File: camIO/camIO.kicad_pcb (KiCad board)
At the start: 4 copper layers, 30 x 30 mm, 37 parts, among them IC3 TLV61225DC, J6 MISC, J8 CSI/DSI, Q1 BSS138, U1 PCA9306

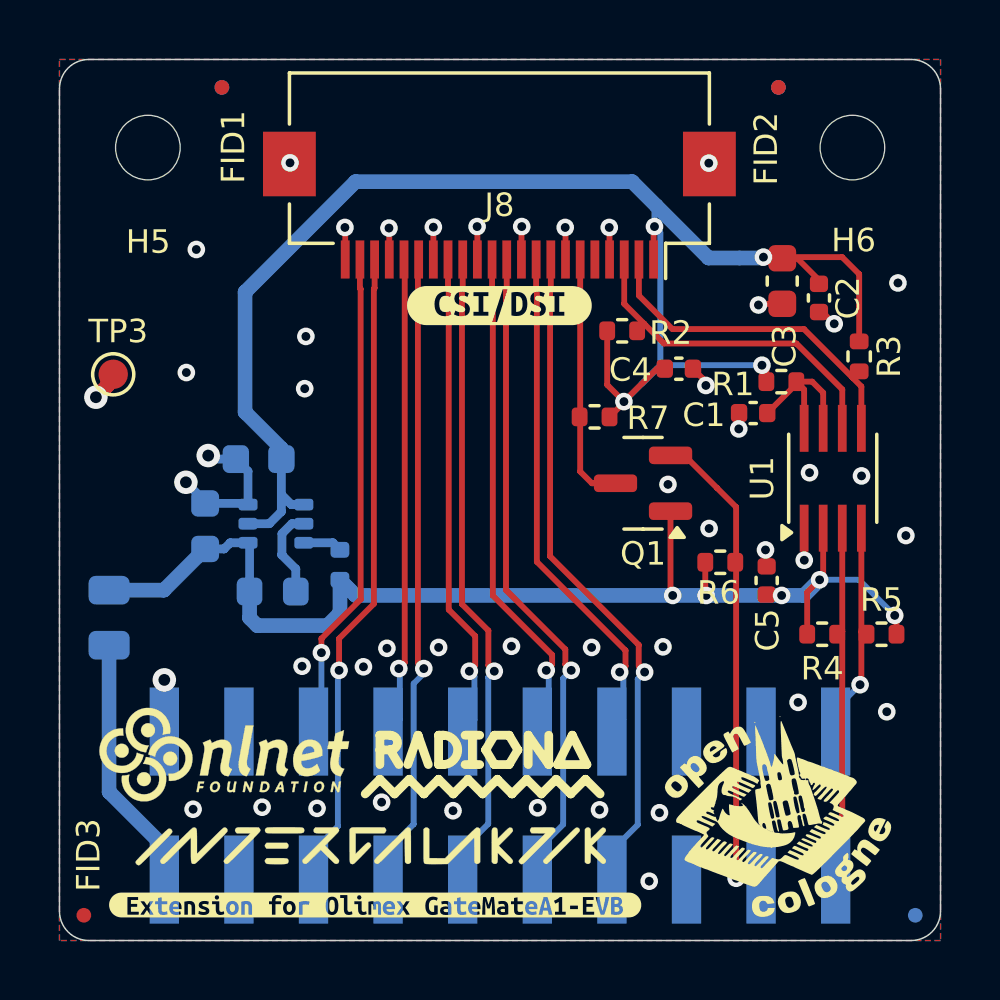
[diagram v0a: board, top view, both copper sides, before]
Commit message: Removing U1 as it is not needed - #4
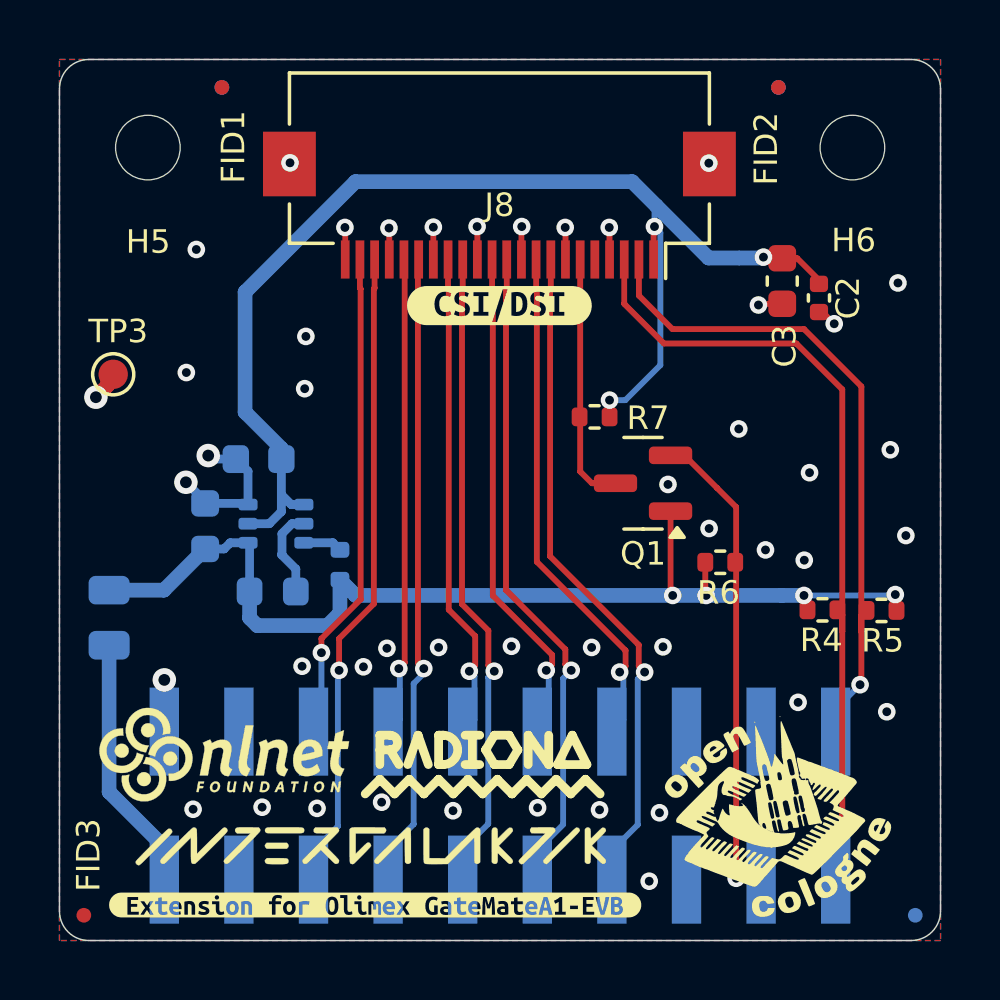
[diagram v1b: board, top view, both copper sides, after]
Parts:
- removed C1: 470p, Capacitor_SMD:C_0402_1005Metric
- removed C4, C5: 100n, Capacitor_SMD:C_0402_1005Metric
- removed R1: 100K, Resistor_SMD:R_0402_1005Metric
- removed R2, R3: 4k7, Resistor_SMD:R_0402_1005Metric
- removed U1: PCA9306, Package_SO:SSOP-8_2.95x2.8mm_P0.65mm
- moved R4 0.83 mm to (111.2, 70.6)
- moved R5 0.81 mm to (113.2, 70.6)
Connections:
- J8 pad 2: /Main Sheet/SDA0 -> /Main Sheet/NB_B8_8N
- J8 pad 3: /Main Sheet/SCL0 -> /Main Sheet/NB_A8_8P
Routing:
- net +VCC_HIGH: track 57.9 -> 42.3 mm, vias 4 -> 3
- net /Main Sheet/NB_B8_8N: track 7.50 -> 23.0 mm
- net /Main Sheet/NB_A8_8P: track 12.5 -> 28.0 mm
- net /Main Sheet/SDA0: track 11.8 -> 0.00 mm
- net /Main Sheet/SCL0: track 11.8 -> 0.00 mm
- net /Main Sheet/VREF2: track 5.47 -> 0.00 mm
- net +VCC_LOW: track 41.4 -> 36.8 mm, vias 5 -> 4
- net GND: track 20.1 -> 17.2 mm, vias 47 -> 46

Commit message: sch cleanup - reference cleanup
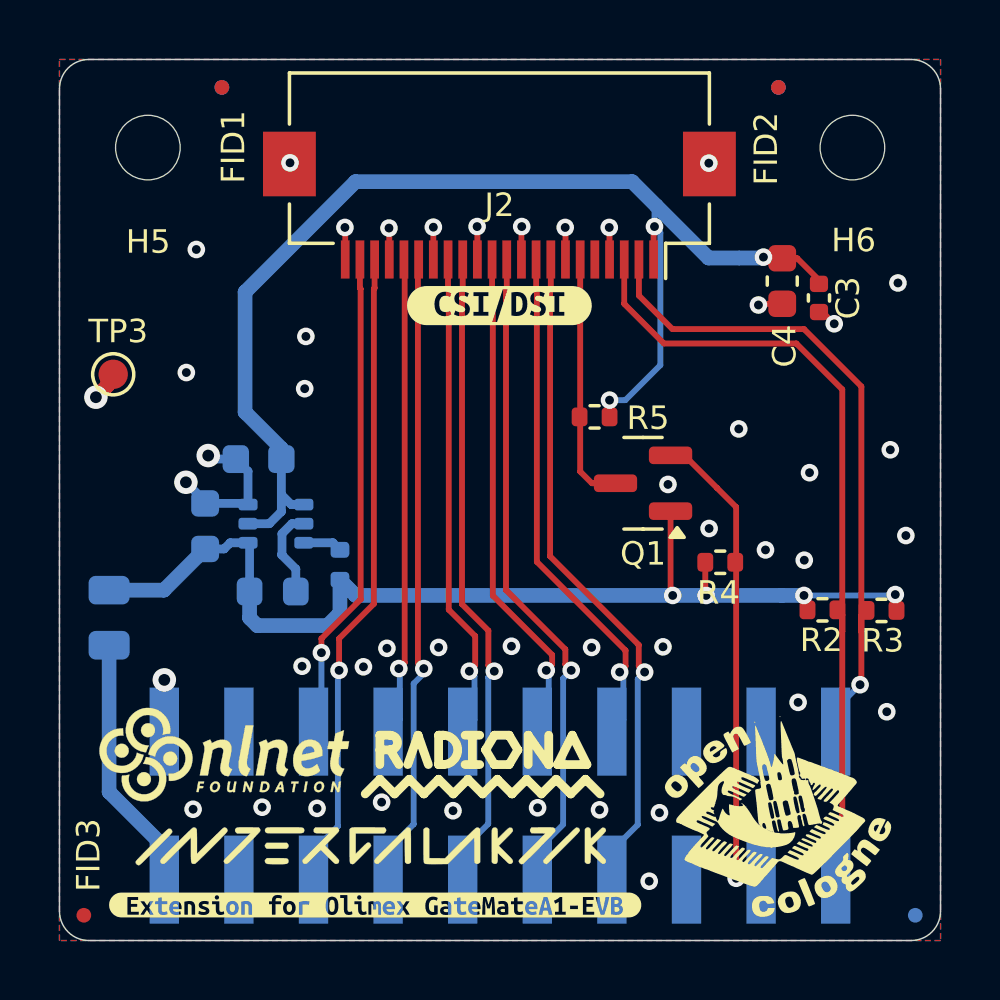
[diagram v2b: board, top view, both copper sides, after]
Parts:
- renumbered C13 to C1, C14 to C2, C2 to C3, C3 to C4, IC3 to IC1, J6 to J1, J8 to J2, R15 to R1, R4 to R2, R5 to R3, R6 to R4, R7 to R5
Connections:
- net /Main Sheet/CAM_C_N renamed /Main Sheet/NB_B3_3N
- net /Main Sheet/CAM_C_P renamed /Main Sheet/NB_A3_3P
- net /Main Sheet/CAM_D0_N renamed /Main Sheet/NB_B1_1N
- net /Main Sheet/CAM_D0_P renamed /Main Sheet/NB_A1_1P
- net /Main Sheet/CAM_D1_N renamed /Main Sheet/NB_B2_2N
- net /Main Sheet/CAM_D1_P renamed /Main Sheet/NB_A2_2P
- net /Main Sheet/CAM_D2_N renamed /Main Sheet/NB_B4_4N
- net /Main Sheet/CAM_D2_P renamed /Main Sheet/NB_A4_4P
- net /Main Sheet/CAM_D3_N renamed /Main Sheet/NB_B5_5N
- net /Main Sheet/CAM_D3_P renamed /Main Sheet/NB_A5_5P

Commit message: Adding LP pins on P side of diff pair #4
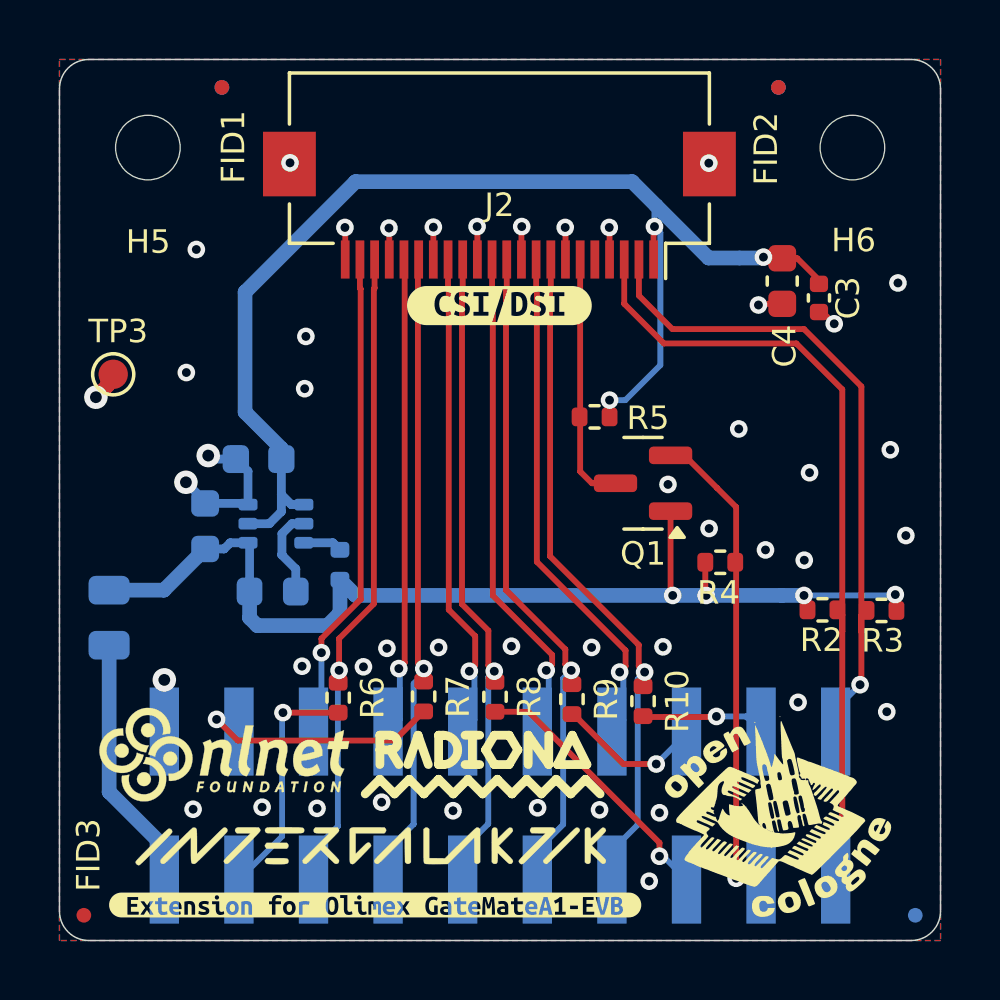
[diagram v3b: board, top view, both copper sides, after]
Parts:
- added R10: 3k3, Resistor_SMD:R_0402_1005Metric, F.Cu at (105.1, 73.7)
- added R6: 3k3, Resistor_SMD:R_0402_1005Metric, F.Cu at (94.7, 73.6)
- added R7: 3k3, Resistor_SMD:R_0402_1005Metric, F.Cu at (97.7, 73.5)
- added R8: 3k3, Resistor_SMD:R_0402_1005Metric, F.Cu at (100.1, 73.5)
- added R9: 3k3, Resistor_SMD:R_0402_1005Metric, F.Cu at (102.7, 73.6)
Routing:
- net /Main Sheet/NB_A6_6P: track 0.00 -> 9.16 mm, vias 0 -> 1
- net /Main Sheet/NB_B0_0N: track 0.00 -> 8.69 mm, vias 0 -> 1
- net /Main Sheet/NB_A0_0P: track 0.00 -> 8.19 mm, vias 0 -> 1
- net /Main Sheet/NB_B6_6N: track 0.00 -> 5.11 mm, vias 0 -> 1
- net /Main Sheet/NB_B7_7N: track 0.00 -> 4.25 mm, vias 0 -> 1

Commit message: Adding termination #4
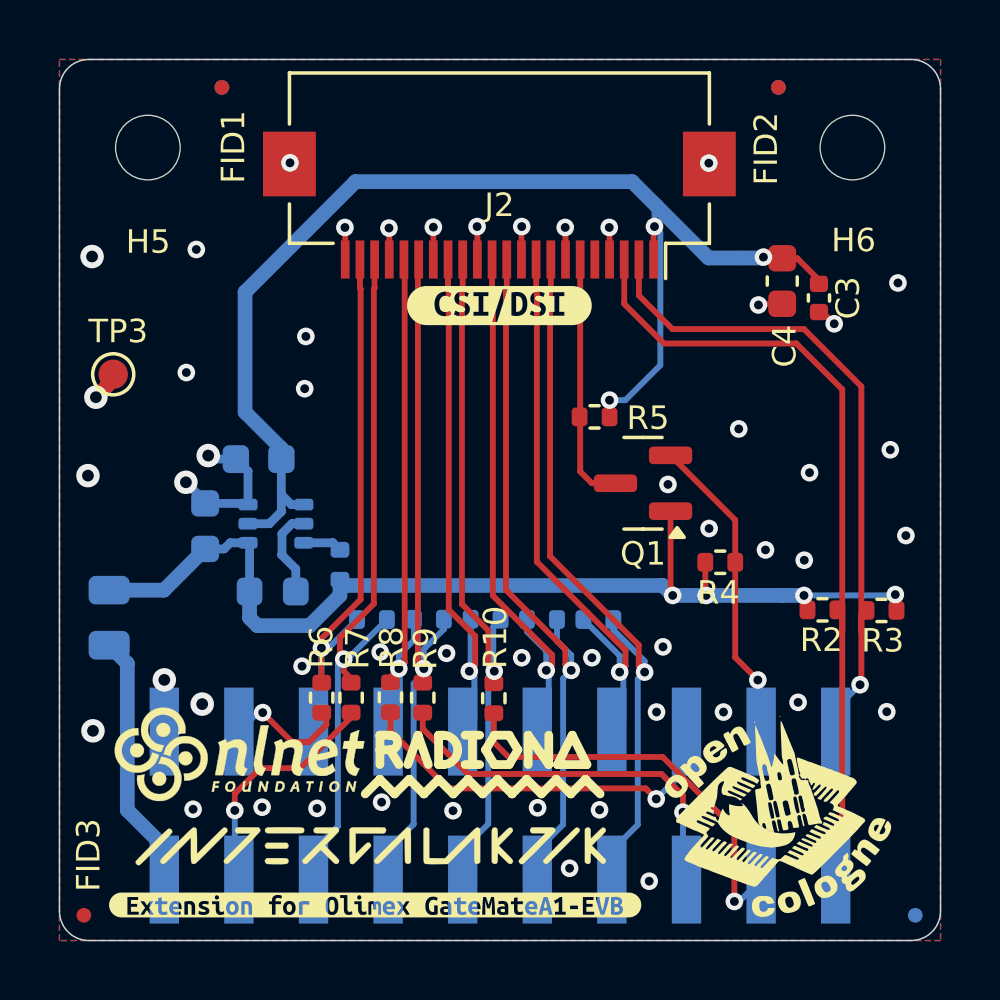
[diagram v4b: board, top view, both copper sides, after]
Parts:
- added R11: 100, Resistor_SMD:R_0402_1005Metric, B.Cu at (95.9, 70.9)
- added R12: 100, Resistor_SMD:R_0402_1005Metric, B.Cu at (97.8, 70.9)
- added R13: 100, Resistor_SMD:R_0402_1005Metric, B.Cu at (99.8, 70.9)
- added R14: 100, Resistor_SMD:R_0402_1005Metric, B.Cu at (101.7, 70.9)
- added R15: 100, Resistor_SMD:R_0402_1005Metric, B.Cu at (103.6, 70.9)
- R10, R6, R7, R8, R9: value 3k3 -> 100
- moved R10 5.08 mm to (100.0, 73.6)
- moved R9 5.08 mm to (97.6, 73.6)
- moved R8 3.56 mm to (96.5, 73.6)
- moved R7 2.47 mm to (95.2, 73.6)
- moved R6 0.56 mm to (94.2, 73.6)
- moved H2 0.52 mm to (91.4, 75.5)
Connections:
- Q1 pad 2: /Main Sheet/NB_A7_7P -> /Main Sheet/NB_B7_7N
- R10 pad 1: /Main Sheet/NB_A5_5P -> /Main Sheet/NB_A3_3P
- R10 pad 2: /Main Sheet/NB_B7_7N -> /Main Sheet/NB_A7_7P
- R4 pad 1: /Main Sheet/NB_A7_7P -> /Main Sheet/NB_B7_7N
- R6 pad 1: /Main Sheet/NB_A1_1P -> /Main Sheet/NB_B1_1N
- R6 pad 2: /Main Sheet/NB_A0_0P -> /Main Sheet/NB_B0_0N
- R7 pad 1: /Main Sheet/NB_A2_2P -> /Main Sheet/NB_A1_1P
- R7 pad 2: /Main Sheet/NB_B0_0N -> /Main Sheet/NB_A0_0P
- R8 pad 1: /Main Sheet/NB_A3_3P -> /Main Sheet/NB_B2_2N
- R8 pad 2: /Main Sheet/NB_A6_6P -> /Main Sheet/NB_B6_6N
- R9 pad 1: /Main Sheet/NB_A4_4P -> /Main Sheet/NB_A2_2P
- R9 pad 2: /Main Sheet/NB_B6_6N -> /Main Sheet/NB_A6_6P
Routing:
- net /Main Sheet/NB_B6_6N: track 5.11 -> 13.4 mm
- net /Main Sheet/NB_B7_7N: track 4.25 -> 10.7 mm
- net /Main Sheet/NB_B0_0N: track 8.69 -> 4.38 mm
- net /Main Sheet/NB_A6_6P: track 9.16 -> 13.3 mm
- net /Main Sheet/NB_B1_1N: track 16.8 -> 19.5 mm
- net /Main Sheet/NB_A1_1P: track 22.4 -> 25.0 mm
- net /Main Sheet/NB_B2_2N: track 16.3 -> 18.8 mm
- net /Main Sheet/NB_A7_7P: track 16.5 -> 14.1 mm
- net /Main Sheet/NB_B5_5N: track 17.6 -> 19.9 mm
- net /Main Sheet/NB_A2_2P: track 22.2 -> 24.2 mm
- net /Main Sheet/NB_B4_4N: track 17.2 -> 19.2 mm
- net /Main Sheet/NB_A3_3P: track 22.4 -> 24.4 mm
- net /Main Sheet/NB_B3_3N: track 16.8 -> 18.6 mm
- net /Main Sheet/NB_A5_5P: track 23.4 -> 25.2 mm
- net /Main Sheet/NB_A4_4P: track 23.0 -> 24.5 mm
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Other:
- board text added: "Diff termination"
